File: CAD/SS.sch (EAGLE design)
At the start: 113 parts, among them Q1 SN74AHC-NOR, Q2 UMD5N, Q4 SN74AHC-AND, Q5 BFP460, Q6 TCR1HF50, Q7 NCP553, T1 MMBTRA104SS, X1 ANTENNA, X2 RADIO, X3 INP, X4 AMP-O, X5 BPF-O

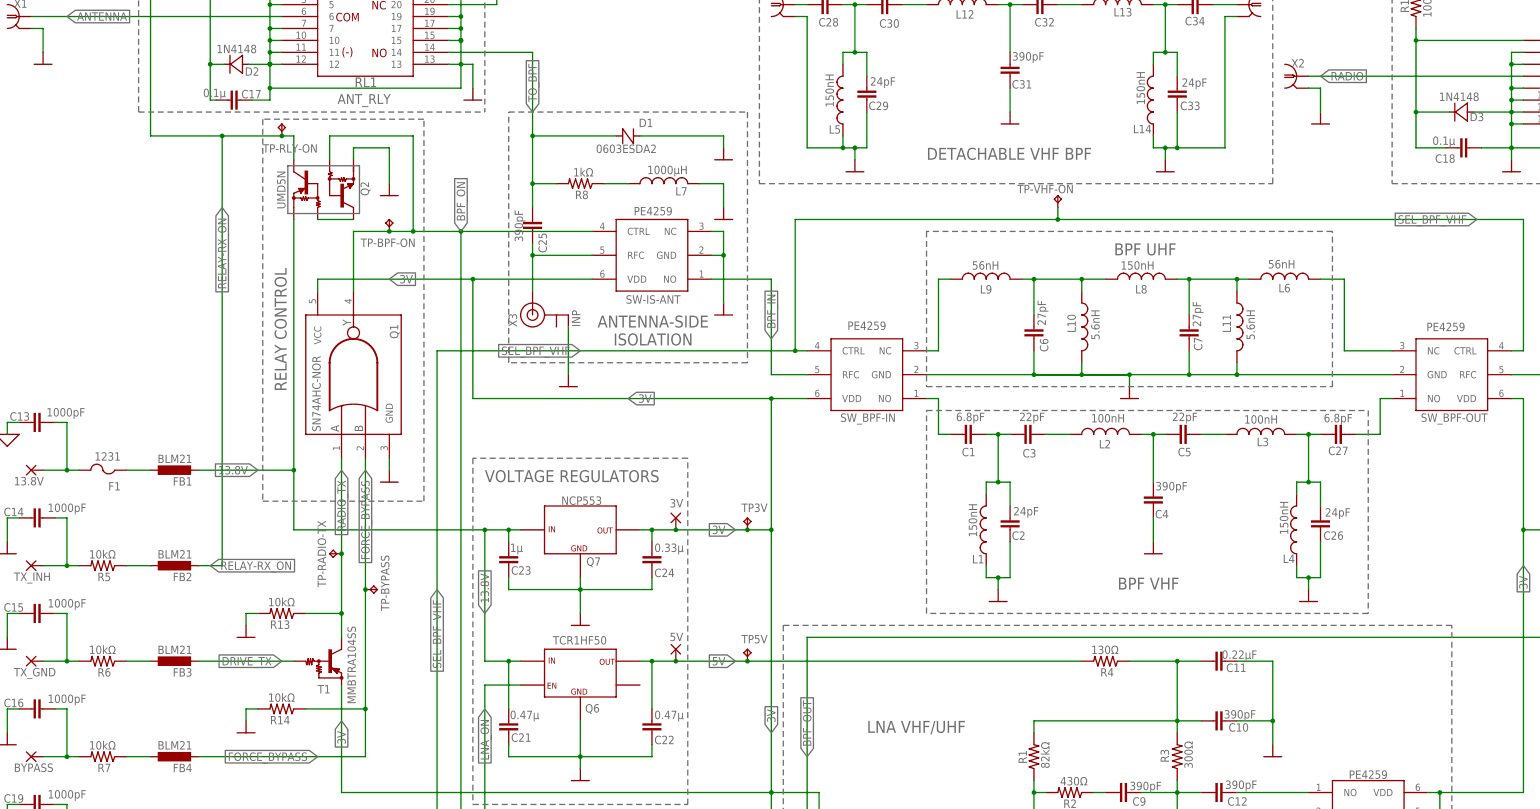
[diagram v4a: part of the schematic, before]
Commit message: Board: Changed pads to jumpers
Why I didn't do it before, doh. Pads are... Complicated.

Also:

- Changed the silk of the fuse (now with value)
- Relabeled the region around the jumper
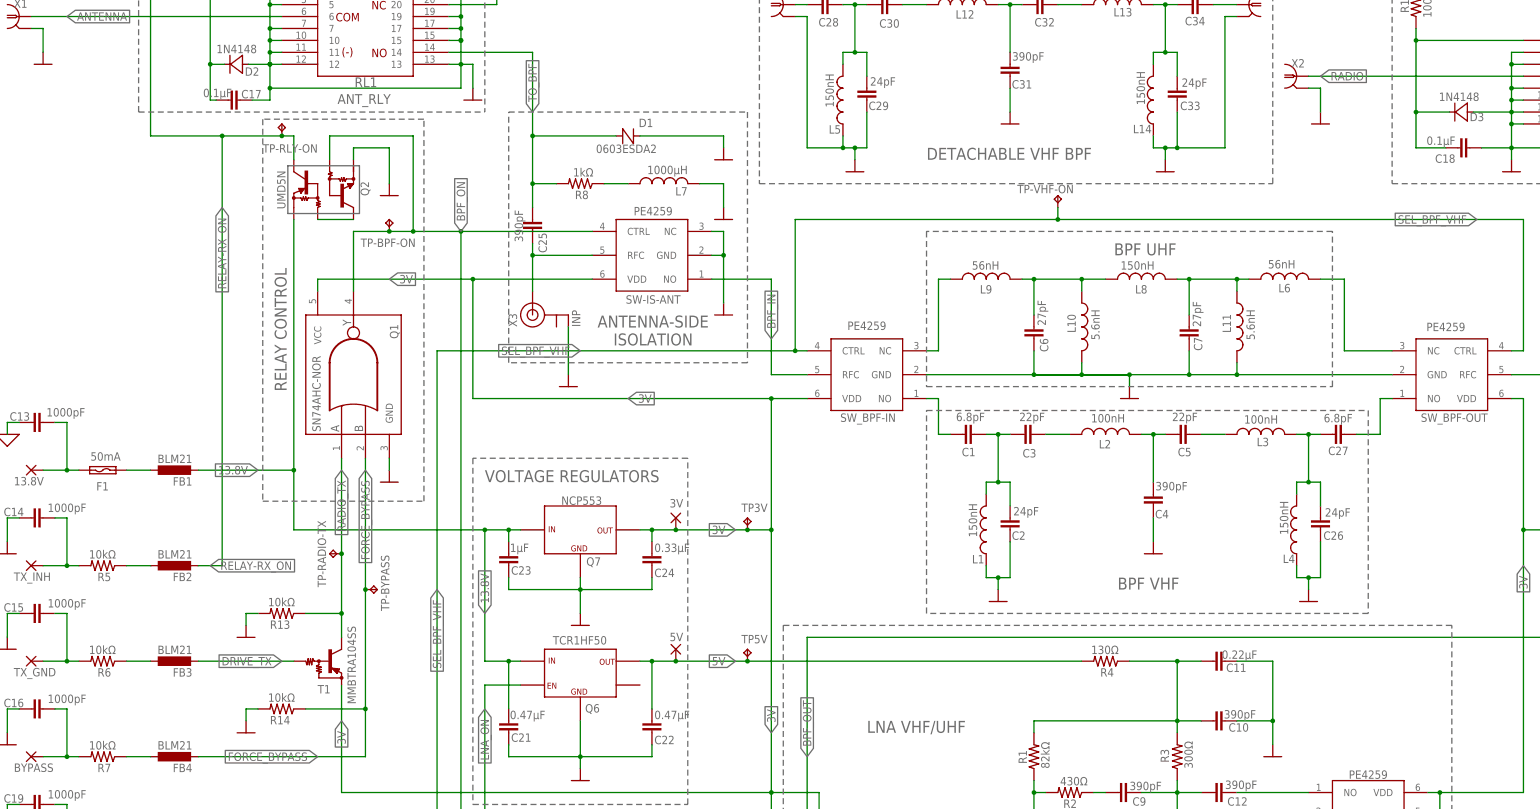
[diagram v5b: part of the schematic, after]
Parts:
- 13.8V, 3V, 5V, AMP_ON, BYPASS, GND, TX_GND, TX_INH, VHF: device wirepad:SMD2 -> aarf:JUMPER-1
- C17, C18: value 0.1µ -> 0.1µF
- C21, C22: value 0.47µ -> 0.47µF
- C23: value 1µ -> 1µF
- C24: value 0.33µ -> 0.33µF
- F1: value 1231 -> 50mA; device adafruit:PTCFUSE-1206 -> aarf:FUSE-1206

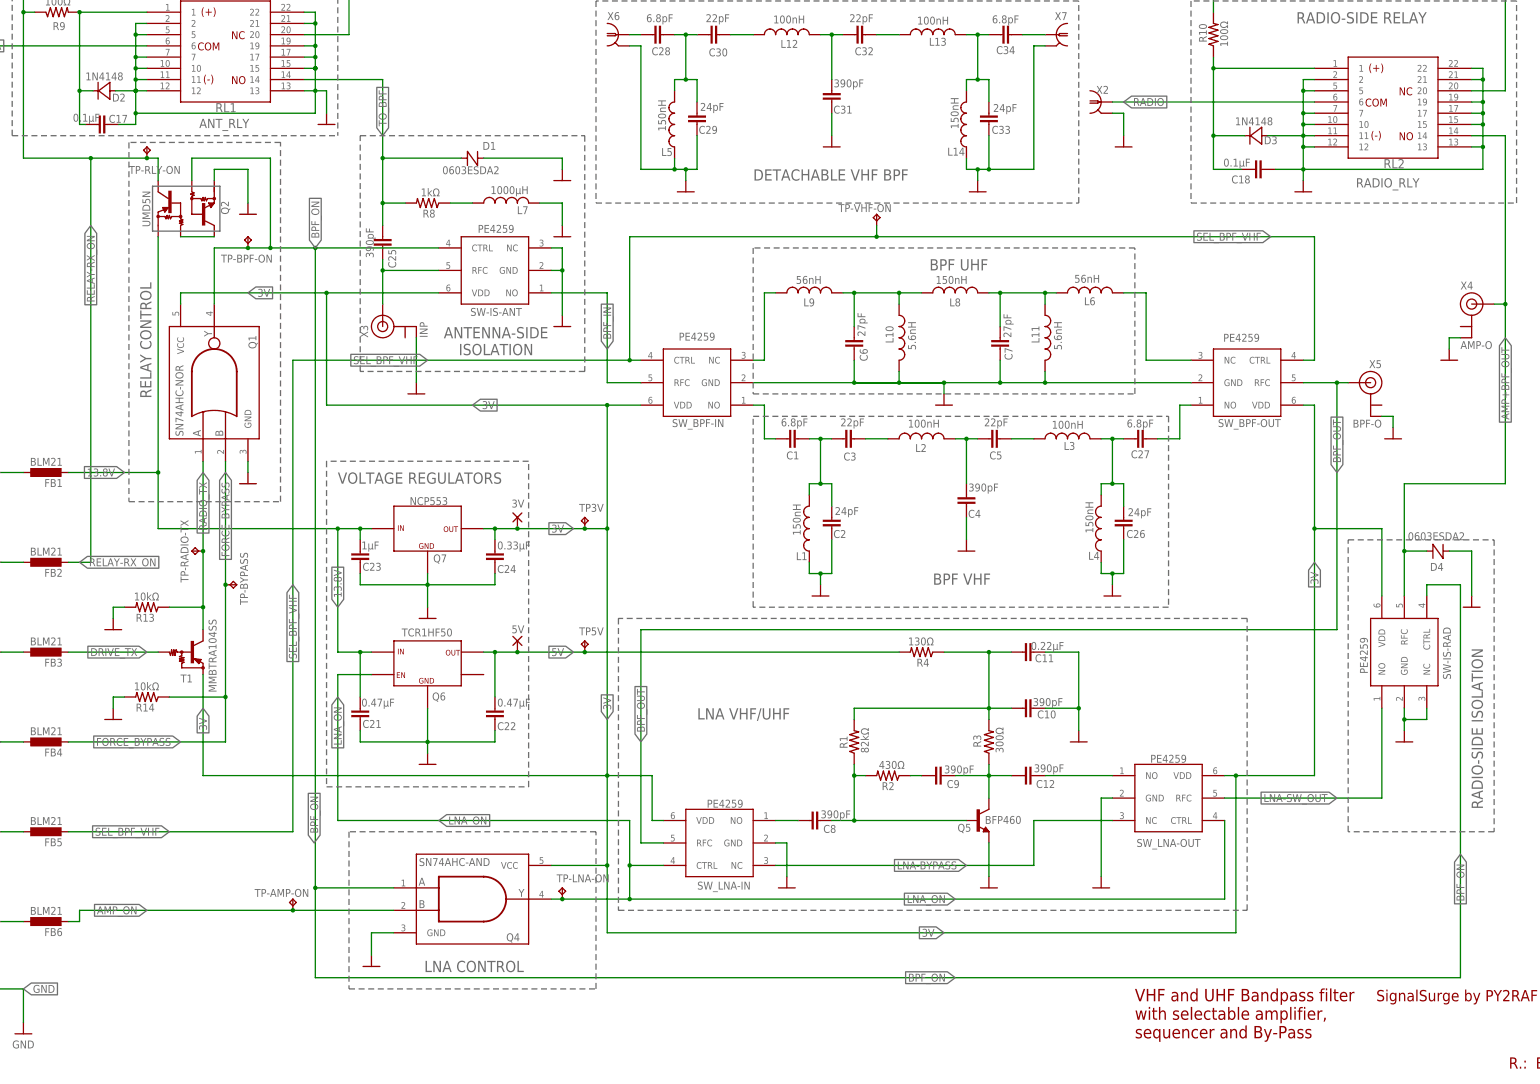
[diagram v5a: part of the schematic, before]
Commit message: Rev. B: Improvements
* Added pulldown lines in comparators
* Routing change on the back of the board
* Unified logic ICs into SC70-5 footprint
* Updated BOM to add new pulldown resistors - fixed wrong 0.22µf part (it was 0.022µf) in BOM
* Better footprint for BFP460 and NCP553
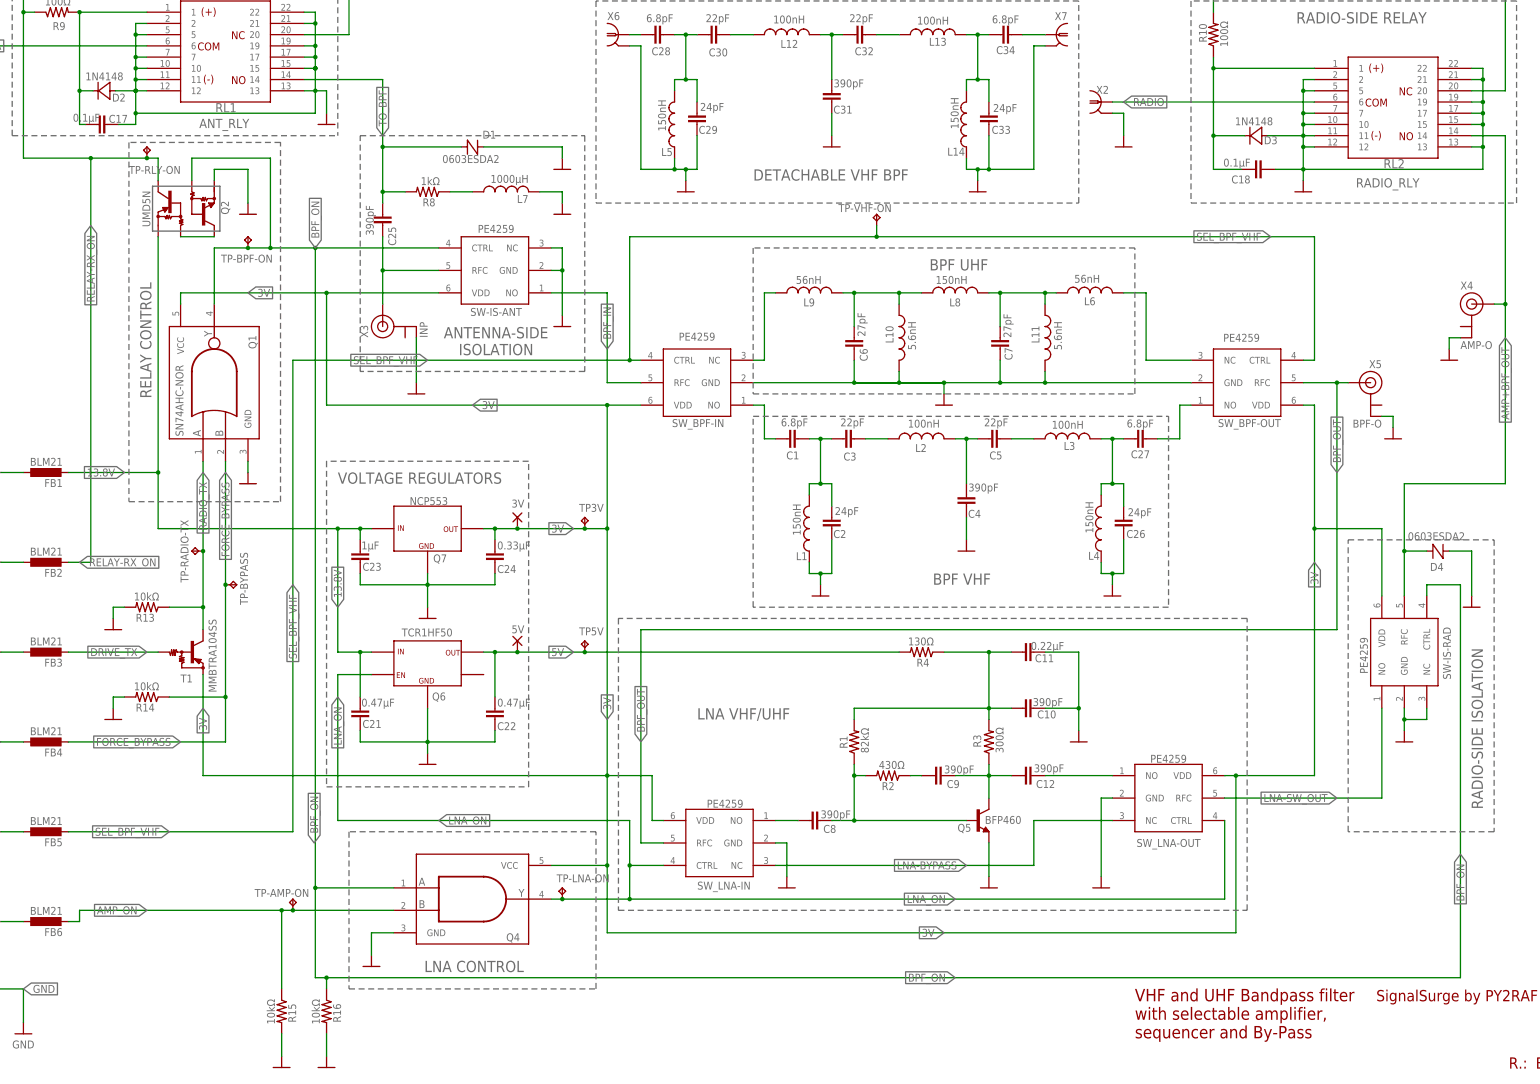
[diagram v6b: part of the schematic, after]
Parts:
- added R15, R16: 10kΩ, aarf:R-1206
- Q4: value SN74AHC-AND -> (none)
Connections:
- net N$10 renamed BYPASS_SEL_IN
- net N$12 renamed VHF_ON_IN
- net N$15 renamed AMP_ON_IN
- net N$16 renamed TX_GND_IN
- net N$2 renamed BLEED
- net N$26 renamed TX_INH_OUT
- net N$9 renamed 13.8V_IN
- net AMP_ON: now also R15.1
- net BPF_ON: now also R16.1
- net GND: now also R15.2, R16.2
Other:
- moved on the sheet: C25, D1, L7, R8

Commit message: Revision C: Initial launch
For more information, check the changelog.
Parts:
- removed C33: 24pF, aarf:MURATACAP
- removed C34: 6.8pF, aarf:MURATACAP
- added L15: 56nH, aarf:L-0805
- added L16, L17: 5.6nH, aarf:L-0805
- added X2A, X2B: (no value), aarf:SMA-EDGE
- C1: value 6.8pF -> 4.7pF; device aarf:MURATACAP -> aarf:C-0805
- C10, C12, C25, C6, C7, C8, C9: device aarf:MURATACAP -> aarf:C-0805
- C2, C29: value 24pF -> 15pF; device aarf:MURATACAP -> aarf:C-0805
- C26: value 24pF -> 4.7pF; device aarf:MURATACAP -> aarf:C-0805
- C27: value 6.8pF -> 15pF; device aarf:MURATACAP -> aarf:C-0805
- C28: value 6.8pF -> 20pF; device aarf:MURATACAP -> aarf:C-0805
- C3: value 22pF -> 20pF; device aarf:MURATACAP -> aarf:C-0805
- C30, C5: value 22pF -> 4.7pF; device aarf:MURATACAP -> aarf:C-0805
- C31: value 390pF -> 27pF; device aarf:MURATACAP -> aarf:C-0805
- C32: value 22pF -> 27pF; device aarf:MURATACAP -> aarf:C-0805
- C4: value 390pF -> 15pF; device aarf:MURATACAP -> aarf:C-0805
- L1, L14, L4, L5: value 150nH -> 56nH
- L12, L2, L3: value 100nH -> 56nH
- L13: value 100nH -> 150nH
- Q4: value (none) -> SN74AHC-AND
- renumbered X6 to X1A, X7 to X1B
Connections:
- net N$24 renamed BIAS_IN
- removed net 0: C13.1
- removed net N$14: C26.1, C27.1, L3.2, L4.1
- removed net N$18: C28.1, C29.1, C30.2, L5.2
- removed net N$19: C5.2, L3.1
- removed net N$20: C30.1, L12.1
- removed net N$21: C31.1, C32.1, L12.2
- removed net N$23: C33.1, C34.1, L13.2, L14.1
- removed net N$25: C32.2, L13.1
- removed net VHF-IN1: C28.2, X1A.1
- removed net VHF-OUT1: C34.2, X1B.1
- new net BPF_VHF: C1.1, C2.1, C3.1, C4.1, C5.1, L1.2, L2.2, L3.1
- new net N$10: C31.2, L13.1, L15.2, L16.1
- new net N$12: L15.1, X2A.1
- new net N$2: L14.2, X2B.1
- new net N$9: C32.2, L13.2, L14.1, L17.1
- net AMP+BPF_OUT: no longer X4.SIGNAL
- net BPF_IN: now also X3.SIGNAL
- net GND: now also C13.1, C27.2, C28.2, C3.2, C31.1, C32.1, L12.2, L16.2, L17.2, L2.1, L3.2, L4.1, X2A.2, X2B.2; no longer C26.2, C31.2, C33.2, L14.2, L4.2
- net LNA-SW_OUT: now also X4.SIGNAL
- net N$17: no longer X3.SIGNAL
- net N$4: now also C26.1, C27.1, C28.1, C29.1, C30.1, L12.1, L4.2, L5.2; no longer C1.1, C2.1, C3.2, L1.2
- net N$5: now also C26.2, X1A.1; no longer C3.1, L2.1
- net N$6: now also C30.2, X1B.1; no longer C4.1, C5.1, L2.2
- net VHF-OUT: now also C5.2; no longer C27.2
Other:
- note added: "BPF UHF TEST"
- moved on the sheet: C10, C11, C12, C26, C27, C28, C29, C3, C30, C31, C32, C4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

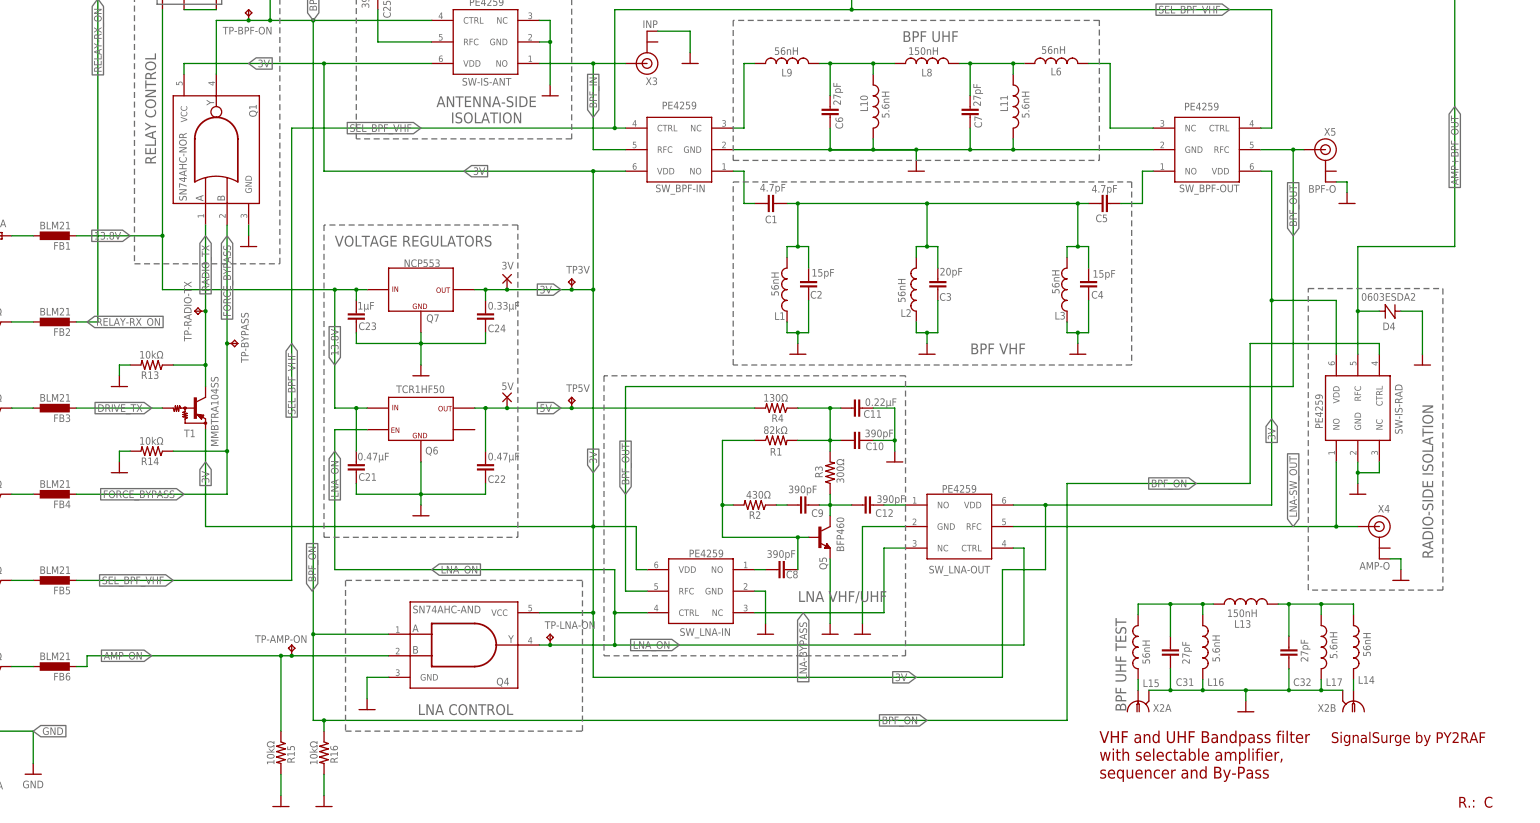
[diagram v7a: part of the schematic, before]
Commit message: Now: Revision D!
- This is now production grade
- Fixed the pesky UMD5N footprint issue
- Documented thoroughly the BPF and Amplifier performance
- Decoupled the relay logic markdown
- Changed pulldowns on 74XX to 100kR
- More silkscreen, ink for the win
- Resolves: #6, #23, #24
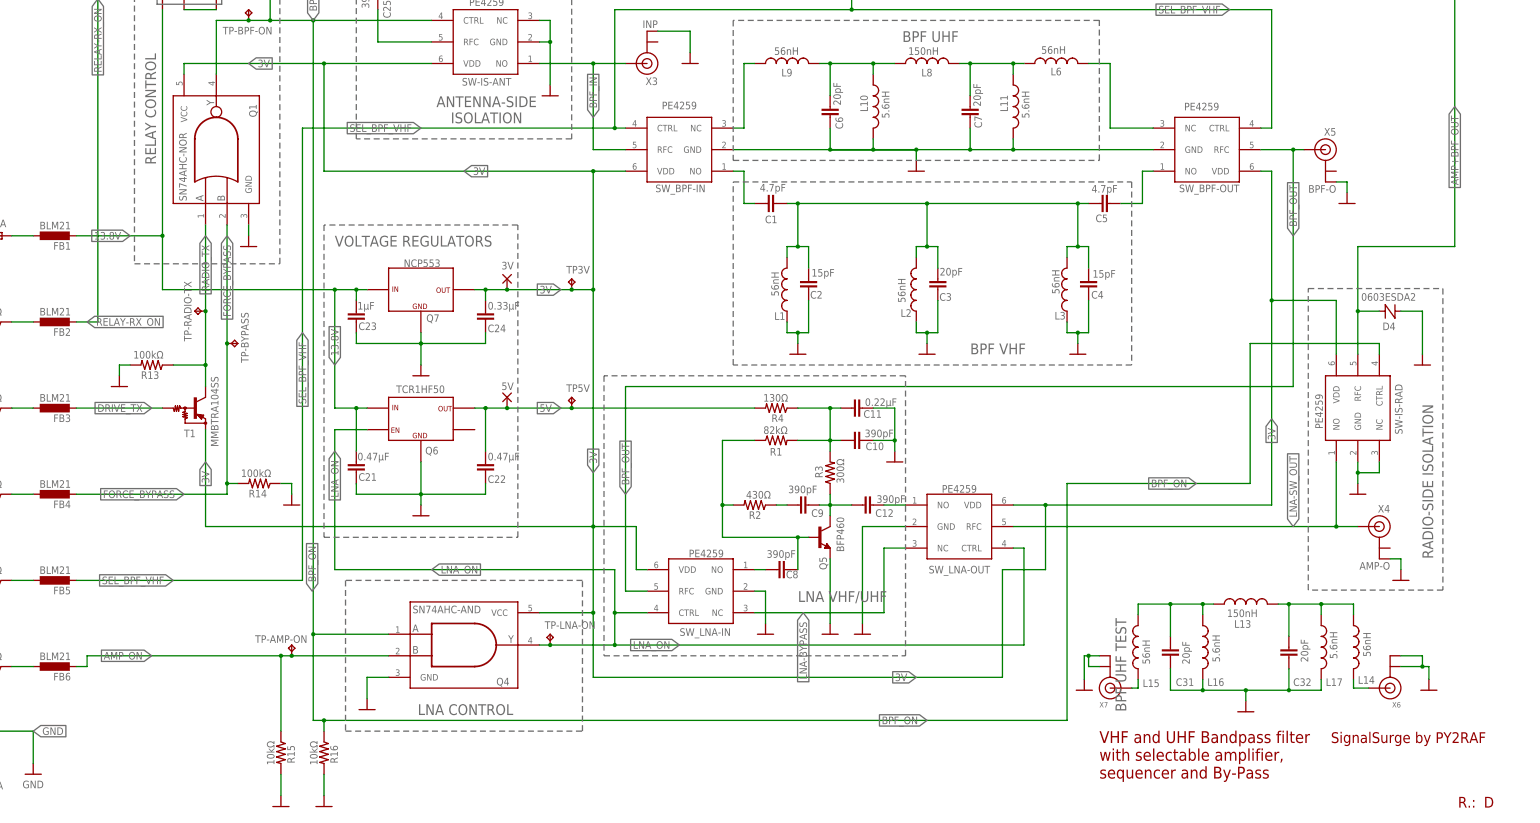
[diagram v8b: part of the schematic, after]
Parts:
- removed X2A, X2B: (no value), aarf:SMA-EDGE
- added X6, X7: (no value), adafruit:ANTENNA_U.FL
- C31, C32, C6, C7: value 27pF -> 20pF
- R13, R14: value 10kΩ -> 100kΩ
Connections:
- net FORCE_BYPASS: now also R14.2; no longer R14.1
- net GND: now also R14.1, X6.GND@0, X6.GND@1, X7.GND@0, X7.GND@1; no longer R14.2, X2A.2, X2B.2
- net N$12: now also L14.2, X6.SIGNAL; no longer L15.1, X2A.1
- net N$2: now also L15.1, X7.SIGNAL; no longer L14.2, X2B.1
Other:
- moved on the sheet: R14
